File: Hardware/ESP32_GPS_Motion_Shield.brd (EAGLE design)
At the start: 25.4 x 50.8 mm, 38 parts, among them J2 MICRO-SD_CARD_SOCKET, J7 BM06B-SRSS-TB, Q1 4.3A/20V/54mΩ, Q2 4.3A/20V/54mΩ, U1 LSM9DS1

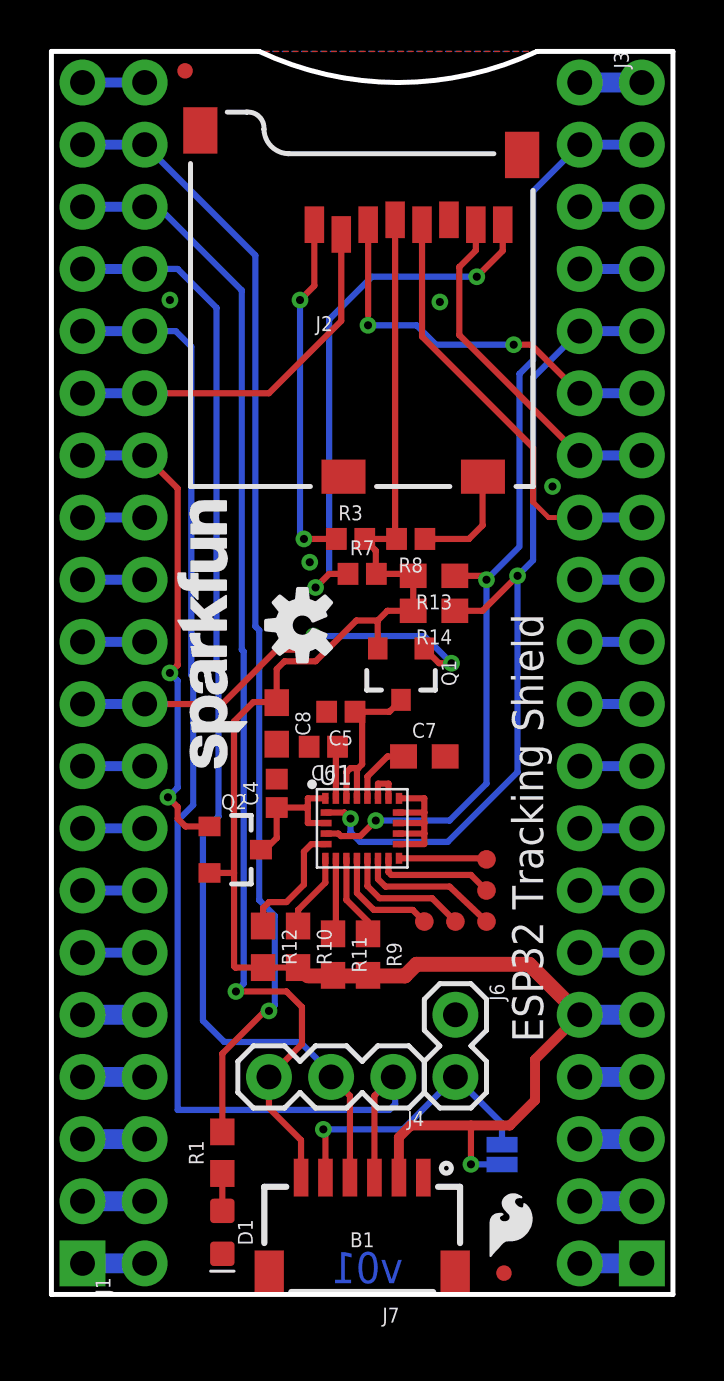
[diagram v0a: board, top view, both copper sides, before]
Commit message: Checked DRC, ready for kickoff
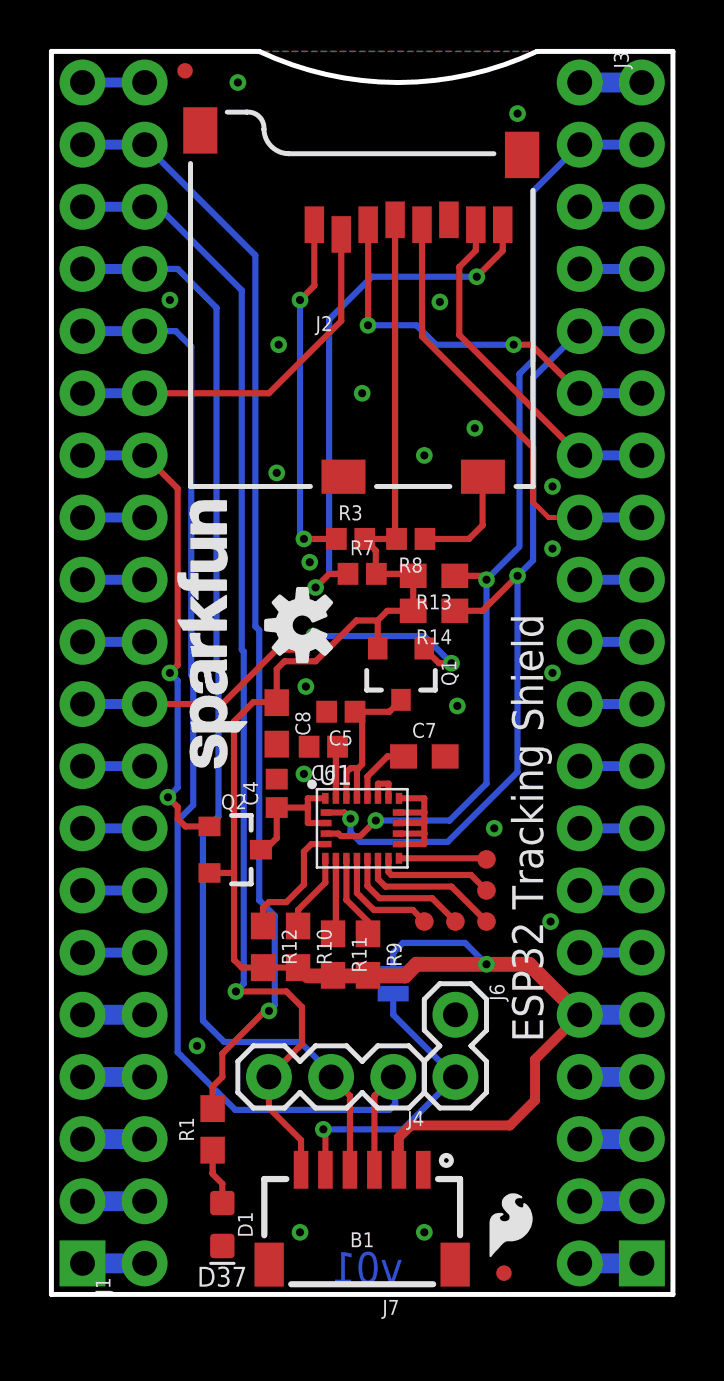
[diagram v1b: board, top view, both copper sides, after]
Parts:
- moved JP1 8.28 mm to (14.0, 12.7), turned to 90 degrees
- moved R1 1.03 mm to (6.59, 6.75)
- moved J7 0.32 mm to (12.7, 0.32)
- moved D1 0.32 mm to (6.99, 2.86)
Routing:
- net 3.3V: track 79.0 -> 80.9 mm
- net GPS_TX: track 50.9 -> 49.2 mm
- net N$1: track 1.53 -> 2.33 mm
- net GPS_LED: track 46.1 -> 45.3 mm
- net N$2: track 11.9 -> 12.4 mm
- net GND: vias 4 -> 21
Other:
- board text added: "!RST!"
- board text added: "0"
- board text added: "12"
- board text added: "13"
- board text added: "14"
- board text added: "15"
- board text added: "16"
- board text added: "17"
- board text added: "18"
- board text added: "19"
- board text added: "2"
- board text added: "21"
- board text added: "22"
- board text added: "23"
- board text added: "25"
- board text added: "26"
- board text added: "27"
- board text added: "32"
- board text added: "33"
- board text added: "34"
- board text added: "35"
- board text added: "36"
- board text added: "37"
- board text added: "38"
- board text added: "39"
- board text added: "3V3"
- board text added: "4"
- board text added: "5"
- board text added: "Close for 3.3V on GPS_BAT"
- board text added: "D37"
- board text added: "GND"
- board text added: "GPS_BAT"
- board text added: "GPS_CTL"
- board text added: "GPS_RX"
- board text added: "GPS_TX"
- board text added: "RXI"
- board text added: "TXO"
- board text added: "VBAT"
- board text added: "VUSB"

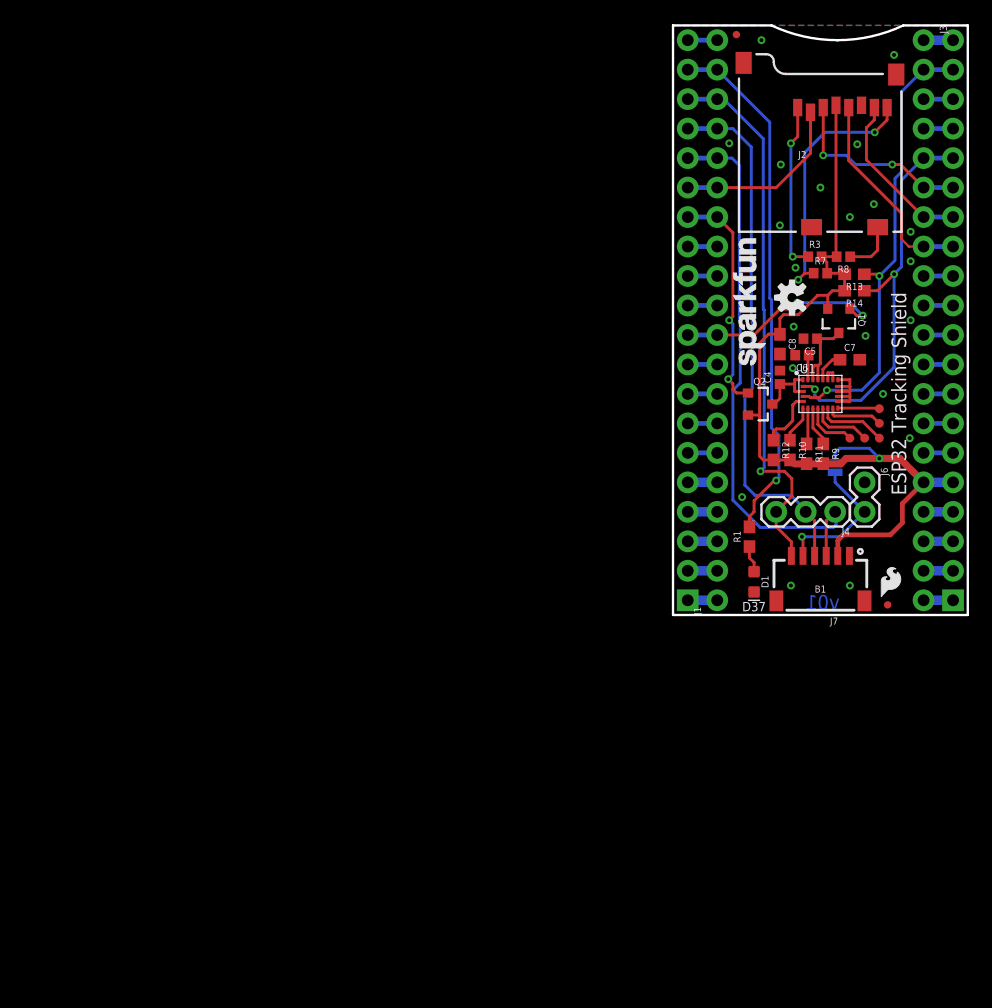
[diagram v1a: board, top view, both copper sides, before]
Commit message: Switched to other GPS jack
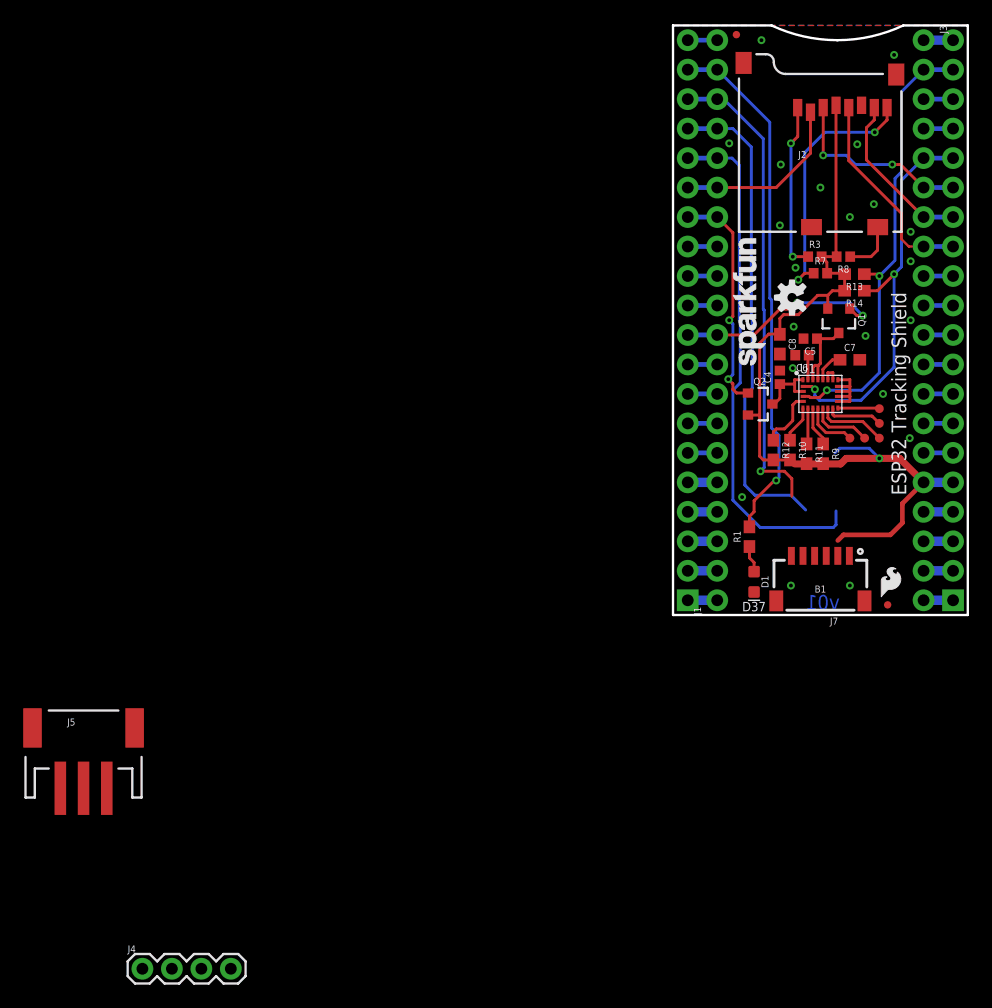
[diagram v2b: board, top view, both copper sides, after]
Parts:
- removed J6: (no value), SparkFun-Connectors:1X02
- removed JP1: JUMPER-SMT_2_NO_SILK, SparkFun-Jumpers:SMT-JUMPER_2_NO_SILK
- added J5: 3-PIN SMD, SparkFun-Connectors:JST-3-SMD
- J4: device SparkFun-Connectors:1X03 -> SparkFun-Connectors:1X04
- moved J4 71.5 mm to (-45.7, -30.5), turned to 0 degrees
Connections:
- removed net N$2: J6.2, J7.5, JP1.1
- net 3.3V: now also J4.4, J5.3; no longer J7.2, JP1.2
- net GND: now also J4.3, J5.2; no longer J6.1, J7.1
- net GPS_CTRL: no longer J4.3, J7.6
- net GPS_RX: now also J4.1; no longer J4.2, J7.4
- net GPS_TX: now also J4.2, J5.1; no longer J4.1, J7.3
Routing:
- net N$2: track 12.4 -> 0.00 mm, vias 1 -> 0
- net GPS_CTRL: track 47.5 -> 41.2 mm
- net GPS_RX: track 46.0 -> 41.7 mm
- net GPS_TX: track 49.2 -> 45.0 mm
- net 3.3V: track 80.9 -> 78.8 mm

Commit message: Ready for review
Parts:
- removed J5: 3-PIN SMD, SparkFun-Connectors:JST-3-SMD
- removed J7: BM06B-SRSS-TB, SparkFun-Connectors:JST-6-SMD-HORI-1.0MM
- added FD3, FD4: FIDUCIALUFIDUCIAL, SparkFun-Aesthetics:FIDUCIAL-MICRO
- added J6: 3-PIN SMD, SparkFun-Connectors:JST-3-SMD
- moved J4 63.2 mm to (8.89, 1.27)
- moved LOGO1 0.67 mm to (10.7, 26.9)
- moved D1 0.64 mm to (6.35, 2.86)
- moved LOGO4 0.57 mm to (8.79, 20.6)
- moved FD1 0.56 mm to (19.1, 0.95)
- moved LOGO3 0.40 mm to (18.0, 1.21)
- moved R1 0.24 mm to (6.35, 6.75)
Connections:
- net 3.3V: now also J6.3; no longer J5.3
- net GND: now also J6.2; no longer J5.2, J7.M1, J7.M2
- net GPS_TX: now also J6.1; no longer J5.1
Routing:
- net GPS_CTRL: track 41.2 -> 2.54 mm, vias 1 -> 0
- net GPS_RX: track 41.7 -> 48.1 mm
- net GPS_TX: track 45.0 -> 49.1 mm, vias 0 -> 1
- net 3.3V: track 78.8 -> 81.1 mm
- net GND: track 21.5 -> 23.6 mm, vias 21 -> 24
- net SD_DI: track 16.5 -> 18.0 mm
- net N$9: track 14.5 -> 15.2 mm
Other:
- board text added: "ESP32 Motion Shield"
- board text removed: "Close for 3.3V on GPS_BAT"
- board text removed: "ESP32 Tracking Shield"
- board text removed: "GPS_BAT"
- board text removed: "GPS_CTL"

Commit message: Ready for QC review
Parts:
- removed LOGO4: SFE_LOGO_NAME.1_INCH, SparkFun-Aesthetics:SFE_LOGO_NAME_.1
- removed R8: 100K, SparkFun-Resistors:0402
- added LOGO2: SFE_LOGO_NAME_FLAME.2_INCH, SparkFun-Aesthetics:SFE_LOGO_NAME_FLAME_.2
- added R2, R4, R5, R6: 10k, SparkFun-Resistors:0603
- moved LOGO1 5.17 mm to (7.43, 30.9), turned to 0 degrees
- moved R13 3.02 mm to (16.8, 26.6), turned to 90 degrees
- moved R14 3.02 mm to (18.3, 26.6), turned to 90 degrees
- moved R3 2.25 mm to (10.0, 30.6), turned to 270 degrees
- moved R7 1.46 mm to (11.4, 30.0), turned to 270 degrees
- moved R11 0.08 mm to (11.5, 14.0)
- moved R9 0.08 mm to (12.9, 14.0)
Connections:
- removed net GPS_CTRL: B1.18, J1.18
- removed net N$11: J2.CD1, R8.1
- new net 3.3V_B: B1.5, J1.5
- new net SD_CD: B1.18, J1.18, J2.CD2
- new net VUSB_B: B1.2, J1.2
- new net V_BATT_B: B1.3, J1.3
- net 3.3V: now also R2.2, R4.2, R5.2, R6.2; no longer B1.5, J1.5, R8.2
- net GND: now also J2.CD1
- net SD_CS: now also R2.1
- net SD_DO: now also R4.1
- net VDDIO_CTRL: now also R5.1
- net VDD_CTRL: now also R6.1
- net VUSB: no longer B1.2, J1.2
- net V_BATT: no longer B1.3, J1.3
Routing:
- net SD_CD: track 0.00 -> 21.6 mm, vias 0 -> 2
- net SD_CS: track 15.1 -> 26.2 mm, vias 0 -> 2
- net SD_DO: track 14.3 -> 22.6 mm, vias 0 -> 2
- net N$11: track 4.58 -> 0.00 mm
- net VDDIO_CTRL: track 20.0 -> 24.0 mm
- net 3.3V: track 81.1 -> 84.9 mm, vias 1 -> 0
- net N$10: track 22.1 -> 18.7 mm
- net V_BATT_B: track 0.00 -> 2.54 mm
- net V_BATT: track 5.08 -> 2.54 mm
- net VUSB_B: track 0.00 -> 2.54 mm
- net VUSB: track 5.08 -> 2.54 mm
- net GPS_CTRL: track 2.54 -> 0.00 mm
- net 3.3V_B: track 0.00 -> 2.54 mm
- net N$2: track 2.54 -> 0.00 mm
- net N$9: track 15.2 -> 12.9 mm
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
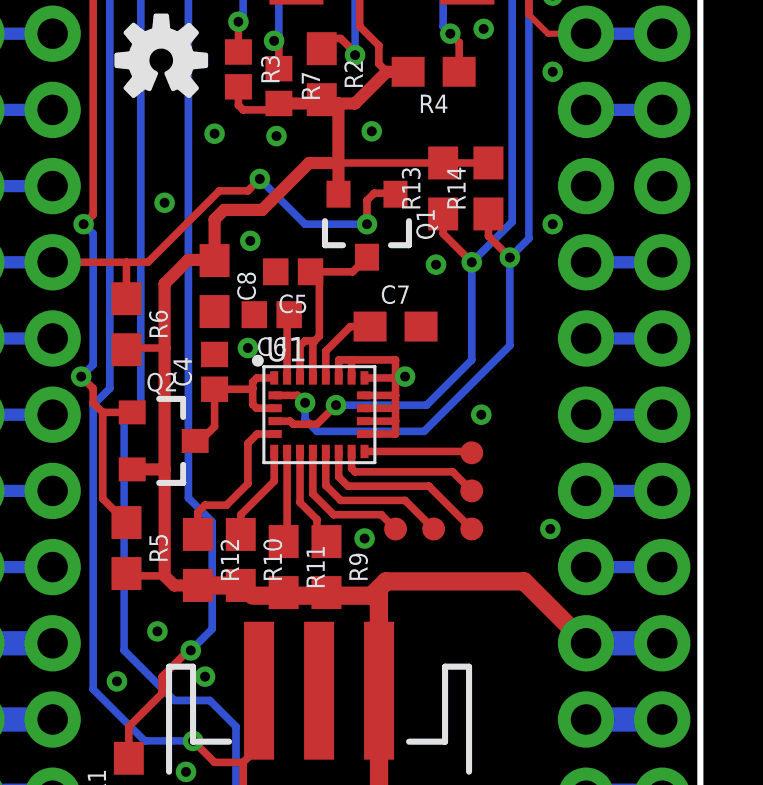
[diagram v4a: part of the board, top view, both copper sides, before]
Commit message: Fixed v01 check issues
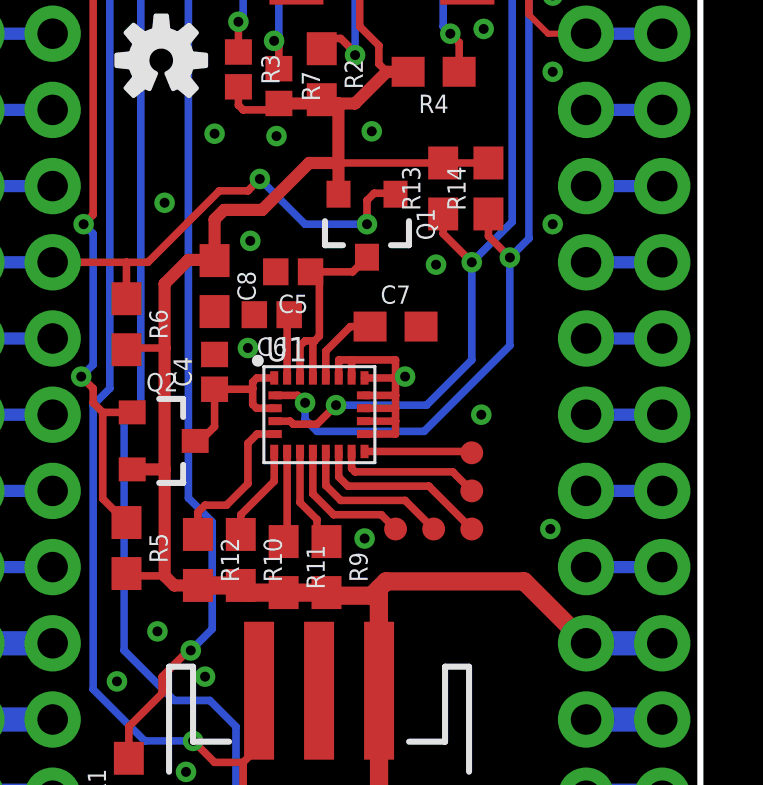
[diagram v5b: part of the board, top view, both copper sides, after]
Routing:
- net N$2: track 0.00 -> 2.54 mm
- net 3.3V: track 84.9 -> 82.4 mm
